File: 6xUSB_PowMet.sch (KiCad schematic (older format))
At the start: 56 parts, among them IC1 ATMEGA32-M, P1 USB_A, P2 USB_A, P3 USB_A, P4 USB_A, P5 USB_A, P6 USB_A, P7 CONN_01X08, P8 CONN_01X03, P9 CONN_01X02, U1 LM1117MP-2.5, U2 LT6106, U3 LT6106, U4 LT6106, U5 LT6106, U6 LT6106, U7 LT6106

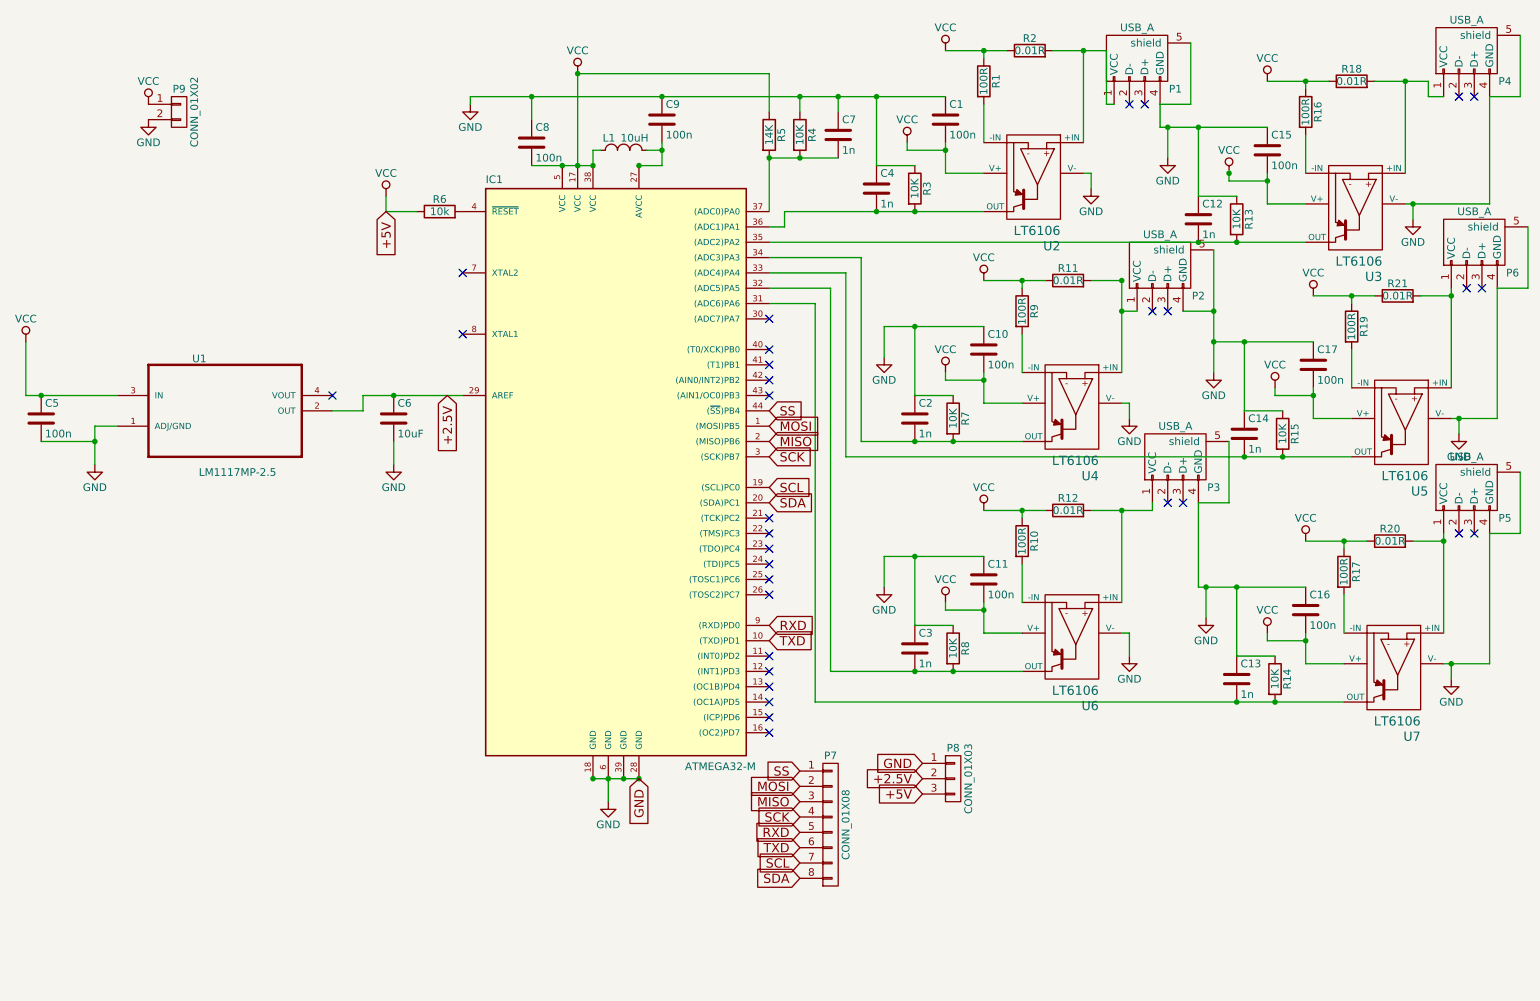
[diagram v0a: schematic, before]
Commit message: Schematic updates
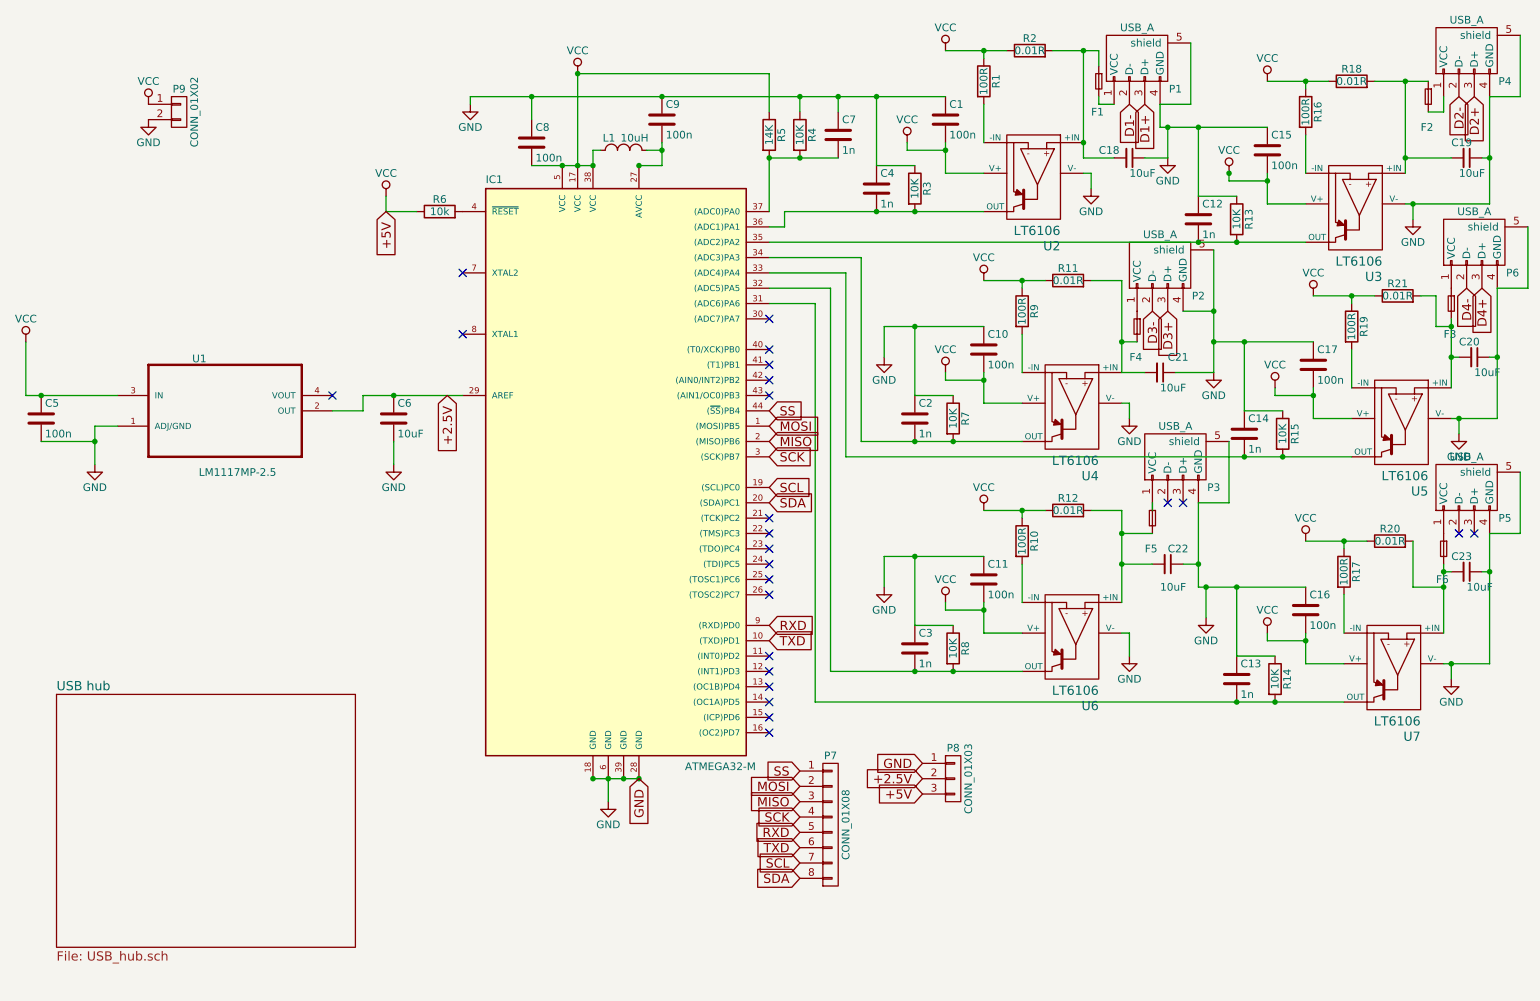
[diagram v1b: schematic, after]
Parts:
- added C18, C19, C20, C21, C22, C23: 10uF, Capacitors_SMD:C_0805_HandSoldering, symbol C_Small
- added F1, F2, F3, F4, F5, F6: F_Small, Fuse_Holders_and_Fuses:Fuse_SMD1206_HandSoldering, symbol F_Small
- P1, P2, P3, P4, P5, P6: footprint Connect:USB_A_Vertical -> USB-A_vertical1:USB_A_Vertical
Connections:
- net GND: now also C18.1, C19.1, C20.1, C21.1, C22.1, C23.1
- net at R2.2, U2.4 (+IN): now also C18.2, F1.1; no longer P1.1 (VCC)
- net at R18.2, U3.4 (+IN): now also C19.2, F2.1; no longer P4.1 (VCC)
- net at R11.2, U4.4 (+IN): now also C21.2, F4.2; no longer P2.1 (VCC)
- net at R21.2, U5.4 (+IN): now also C20.2, F3.2; no longer P6.1 (VCC)
- net at R12.2, U6.4 (+IN): now also C22.2, F5.2; no longer P3.1 (VCC)
- net at R20.2, U7.4 (+IN): now also C23.2, F6.2; no longer P5.1 (VCC)
- net D1-: now reaches P1.2 (D-)
- net D1+: now reaches P1.3 (D+)
- net D2-: now reaches P4.2 (D-)
- net D2+: now reaches P4.3 (D+)
- net D3-: now reaches P2.2 (D-)
- net D3+: now reaches P2.3 (D+)
- net D4-: now reaches P6.2 (D-)
- net D4+: now reaches P6.3 (D+)
- new net: F1.2, P1.1 (VCC)
- new net: F2.2, P4.1 (VCC)
- new net: F4.1, P2.1 (VCC)
- new net: F3.1, P6.1 (VCC)
- new net: F6.1, P5.1 (VCC)
- new net: F5.1, P3.1 (VCC)
- no-connect marks 32 -> 24

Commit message: Schematic updates
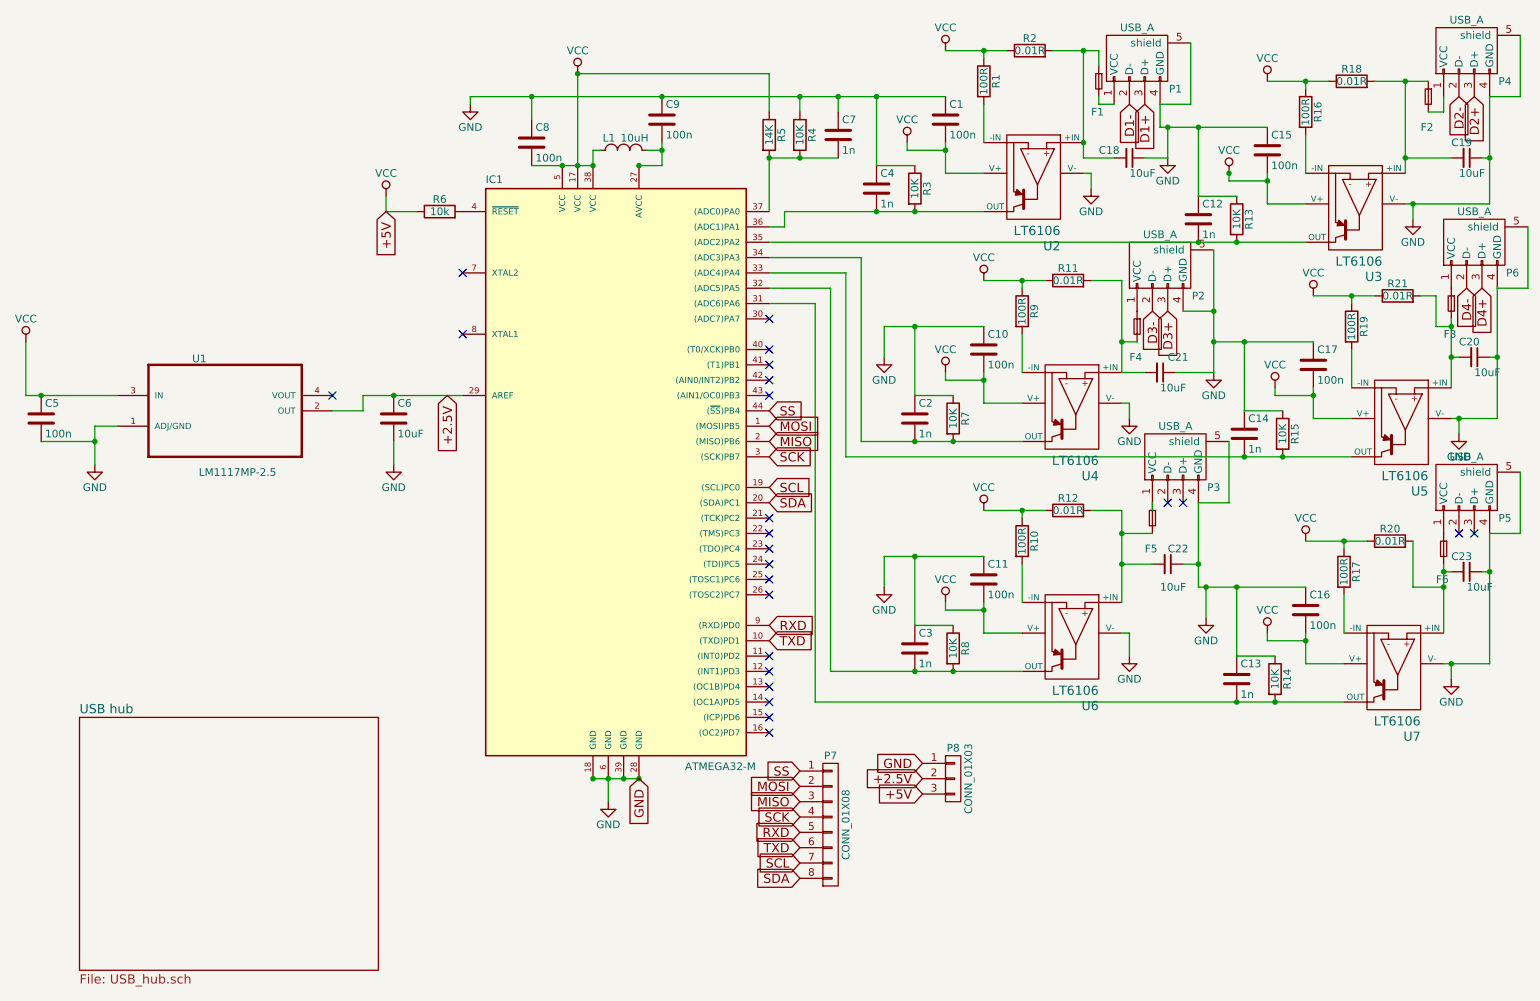
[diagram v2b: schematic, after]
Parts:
- removed P9: CONN_01X02, Connect:BARREL_JACK, symbol CONN_01X02
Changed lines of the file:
@@
 EESchema Schematic File Version 2
+LIBS:TPS5450-EP_DDA_8
 LIBS:power
 LIBS:device
@@
 LIBS:valves
 LIBS:tm-kicad-lib
+LIBS:TPS5450_DDA_8
+LIBS:tom_kicad
 LIBS:6xUSB_PowMet-cache
 EELAYER 25 0
@@
 $EndComp
 $Comp
-L GND #PWR01
+L GND #PWR7
 U 1 1 570DF0BB
 P 4850 6150
-F 0 "#PWR01" H 4850 5900 50  0001 C CNN
+F 0 "#PWR7" H 4850 5900 50  0001 C CNN
 F 1 "GND" H 4850 6000 50  0000 C CNN
 F 2 "" H 4850 6150 50  0000 C CNN
@@
 $EndComp
 $Comp
-L VCC #PWR02
+L VCC #PWR6
 U 1 1 570DF28E
 P 4650 1400
-F 0 "#PWR02" H 4650 1250 50  0001 C CNN
+F 0 "#PWR6" H 4650 1250 50  0001 C CNN
 F 1 "VCC" H 4650 1550 50  0000 C CNN
 F 2 "" H 4650 1400 50  0000 C CNN
@@
 $EndComp
 $Comp
-L VCC #PWR03
+L VCC #PWR1
 U 1 1 570E34BF
 P 1050 3150
-F 0 "#PWR03" H 1050 3000 50  0001 C CNN
+F 0 "#PWR1" H 1050 3000 50  0001 C CNN
 F 1 "VCC" H 1050 3300 50  0000 C CNN
 F 2 "" H 1050 3150 50  0000 C CNN
@@
 $EndComp
 $Comp
-L VCC #PWR04
+L VCC #PWR3
 U 1 1 570E3ABE
 P 3400 2200
-F 0 "#PWR04" H 3400 2050 50  0001 C CNN
+F 0 "#PWR3" H 3400 2050 50  0001 C CNN
 F 1 "VCC" H 3400 2350 50  0000 C CNN
 F 2 "" H 3400 2200 50  0000 C CNN
@@
 $EndComp
 $Comp
-L GND #PWR05
+L GND #PWR5
 U 1 1 570E43D9
 P 3950 1600
-F 0 "#PWR05" H 3950 1350 50  0001 C CNN
+F 0 "#PWR5" H 3950 1350 50  0001 C CNN
 F 1 "GND" H 3950 1450 50  0000 C CNN
 F 2 "" H 3950 1600 50  0000 C CNN
@@
 $EndComp
 $Comp
-L GND #PWR06
+L GND #PWR4
 U 1 1 570E5884
 P 3450 3950
-F 0 "#PWR06" H 3450 3700 50  0001 C CNN
+F 0 "#PWR4" H 3450 3700 50  0001 C CNN
 F 1 "GND" H 3450 3800 50  0000 C CNN
 F 2 "" H 3450 3950 50  0000 C CNN
@@
 $EndComp
 $Comp
-L VCC #PWR07
+L VCC #PWR10
 U 1 1 570E7287
 P 6800 1850
-F 0 "#PWR07" H 6800 1700 50  0001 C CNN
+F 0 "#PWR10" H 6800 1700 50  0001 C CNN
 F 1 "VCC" H 6800 2000 50  0000 C CNN
 F 2 "" H 6800 1850 50  0000 C CNN
@@
 $EndComp
 $Comp
-L VCC #PWR08
+L VCC #PWR11
 U 1 1 570E756C
 P 7050 1250
-F 0 "#PWR08" H 7050 1100 50  0001 C CNN
+F 0 "#PWR11" H 7050 1100 50  0001 C CNN
 F 1 "VCC" H 7050 1400 50  0000 C CNN
 F 2 "" H 7050 1250 50  0000 C CNN
@@
 $EndComp
 $Comp
-L GND #PWR09
+L GND #PWR16
 U 1 1 570E7821
 P 8000 2150
-F 0 "#PWR09" H 8000 1900 50  0001 C CNN
+F 0 "#PWR16" H 8000 1900 50  0001 C CNN
 F 1 "GND" H 8000 2000 50  0000 C CNN
 F 2 "" H 8000 2150 50  0000 C CNN
@@
 $EndComp
 $Comp
-L VCC #PWR010
+L VCC #PWR22
 U 1 1 570E7C8D
 P 8900 2050
-F 0 "#PWR010" H 8900 1900 50  0001 C CNN
+F 0 "#PWR22" H 8900 1900 50  0001 C CNN
 F 1 "VCC" H 8900 2200 50  0000 C CNN
 F 2 "" H 8900 2050 50  0000 C CNN
@@
 $EndComp
 $Comp
-L GND #PWR011
+L GND #PWR28
 U 1 1 570E7CBD
 P 10100 2350
-F 0 "#PWR011" H 10100 2100 50  0001 C CNN
+F 0 "#PWR28" H 10100 2100 50  0001 C CNN
 F 1 "GND" H 10100 2200 50  0000 C CNN
 F 2 "" H 10100 2350 50  0000 C CNN
@@
 $EndComp
 $Comp
-L GND #PWR012
+L GND #PWR19
 U 1 1 570EDB61
 P 8500 1950
-F 0 "#PWR012" H 8500 1700 50  0001 C CNN
+F 0 "#PWR19" H 8500 1700 50  0001 C CNN
 F 1 "GND" H 8500 1800 50  0000 C CNN
 F 2 "" H 8500 1950 50  0000 C CNN
@@
 $EndComp
 $Comp
-L VCC #PWR013
+L VCC #PWR14
 U 1 1 570EDEF6
 P 7300 2750
-F 0 "#PWR013" H 7300 2600 50  0001 C CNN
+F 0 "#PWR14" H 7300 2600 50  0001 C CNN
 F 1 "VCC" H 7300 2900 50  0000 C CNN
 F 2 "" H 7300 2750 50  0000 C CNN
@@
 $EndComp
 $Comp
-L GND #PWR014
+L GND #PWR17
 U 1 1 570EDF0F
 P 8250 3650
-F 0 "#PWR014" H 8250 3400 50  0001 C CNN
+F 0 "#PWR17" H 8250 3400 50  0001 C CNN
 F 1 "GND" H 8250 3500 50  0000 C CNN
 F 2 "" H 8250 3650 50  0000 C CNN
@@
 $EndComp
 $Comp
-L GND #PWR015
+L GND #PWR8
 U 1 1 570EDF17
 P 6650 3250
-F 0 "#PWR015" H 6650 3000 50  0001 C CNN
+F 0 "#PWR8" H 6650 3000 50  0001 C CNN
 F 1 "GND" H 6650 3100 50  0000 C CNN
 F 2 "" H 6650 3250 50  0000 C CNN
@@
 $EndComp
 $Comp
-L VCC #PWR016
+L VCC #PWR25
 U 1 1 570EE269
 P 9200 3450
-F 0 "#PWR016" H 9200 3300 50  0001 C CNN
+F 0 "#PWR25" H 9200 3300 50  0001 C CNN
 F 1 "VCC" H 9200 3600 50  0000 C CNN
 F 2 "" H 9200 3450 50  0000 C CNN
@@
 $EndComp
 $Comp
-L VCC #PWR017
+L VCC #PWR27
 U 1 1 570EE27F
 P 9450 2850
-F 0 "#PWR017" H 9450 2700 50  0001 C CNN
+F 0 "#PWR27" H 9450 2700 50  0001 C CNN
 F 1 "VCC" H 9450 3000 50  0000 C CNN
 F 2 "" H 9450 2850 50  0000 C CNN
@@
 $EndComp
 $Comp
-L GND #PWR018
+L GND #PWR30
 U 1 1 570EE298
 P 10400 3750
-F 0 "#PWR018" H 10400 3500 50  0001 C CNN
+F 0 "#PWR30" H 10400 3500 50  0001 C CNN
 F 1 "GND" H 10400 3600 50  0000 C CNN
 F 2 "" H 10400 3750 50  0000 C CNN
@@
 $EndComp
 $Comp
-L GND #PWR019
+L GND #PWR21
 U 1 1 570EE2A0
 P 8800 3350
-F 0 "#PWR019" H 8800 3100 50  0001 C CNN
+F 0 "#PWR21" H 8800 3100 50  0001 C CNN
 F 1 "GND" H 8800 3200 50  0000 C CNN
 F 2 "" H 8800 3350 50  0000 C CNN
@@
 $EndComp
 $Comp
-L VCC #PWR020
+L VCC #PWR13
 U 1 1 570EE6C7
 P 7050 4850
-F 0 "#PWR020" H 7050 4700 50  0001 C CNN
+F 0 "#PWR13" H 7050 4700 50  0001 C CNN
 F 1 "VCC" H 7050 5000 50  0000 C CNN
 F 2 "" H 7050 4850 50  0000 C CNN
@@
 $EndComp
 $Comp
-L VCC #PWR021
+L VCC #PWR15
 U 1 1 570EE6DD
 P 7300 4250
-F 0 "#PWR021" H 7300 4100 50  0001 C CNN
+F 0 "#PWR15" H 7300 4100 50  0001 C CNN
 F 1 "VCC" H 7300 4400 50  0000 C CNN
 F 2 "" H 7300 4250 50  0000 C CNN
@@
 $EndComp
 $Comp
-L GND #PWR022
+L GND #PWR18
 U 1 1 570EE6F6
 P 8250 5200
-F 0 "#PWR022" H 8250 4950 50  0001 C CNN
+F 0 "#PWR18" H 8250 4950 50  0001 C CNN
 F 1 "GND" H 8250 5050 50  0000 C CNN
 F 2 "" H 8250 5200 50  0000 C CNN
@@
 $EndComp
 $Comp
-L VCC #PWR023
+L VCC #PWR26
 U 1 1 570EEA49
 P 9400 4450
-F 0 "#PWR023" H 9400 4300 50  0001 C CNN
+F 0 "#PWR26" H 9400 4300 50  0001 C CNN
 F 1 "VCC" H 9400 4600 50  0000 C CNN
 F 2 "" H 9400 4450 50  0000 C CNN
@@
 $EndComp
 $Comp
-L GND #PWR024
+L GND #PWR29
 U 1 1 570EEA62
 P 10350 5350
-F 0 "#PWR024" H 10350 5100 50  0001 C CNN
+F 0 "#PWR29" H 10350 5100 50  0001 C CNN
 F 1 "GND" H 10350 5200 50  0000 C CNN
 F 2 "" H 10350 5350 50  0000 C CNN
@@
 $EndComp
 $Comp
-L GND #PWR025
+L GND #PWR20
 U 1 1 570EEA6A
 P 8750 4950
-F 0 "#PWR025" H 8750 4700 50  0001 C CNN
+F 0 "#PWR20" H 8750 4700 50  0001 C CNN
 F 1 "GND" H 8750 4800 50  0000 C CNN
 F 2 "" H 8750 4950 50  0000 C CNN
@@
 +2.5V
 $Comp
-L GND #PWR026
+L GND #PWR9
 U 1 1 57117EE7
 P 6650 4750
-F 0 "#PWR026" H 6650 4500 50  0001 C CNN
+F 0 "#PWR9" H 6650 4500 50  0001 C CNN
 F 1 "GND" H 6650 4600 50  0000 C CNN
 F 2 "" H 6650 4750 50  0000 C CNN
@@
 $EndComp
 $Comp
-L VCC #PWR027
+L VCC #PWR24
 U 1 1 5711831B
 P 9150 5050
-F 0 "#PWR027" H 9150 4900 50  0001 C CNN
+F 0 "#PWR24" H 9150 4900 50  0001 C CNN
 F 1 "VCC" H 9150 5200 50  0000 C CNN
 F 2 "" H 9150 5050 50  0000 C CNN
@@
 NoConn ~ 3050 3500
 $Comp
-L VCC #PWR028
+L VCC #PWR23
 U 1 1 5711A464
 P 9150 1450
-F 0 "#PWR028" H 9150 1300 50  0001 C CNN
+F 0 "#PWR23" H 9150 1300 50  0001 C CNN
 F 1 "VCC" H 9150 1600 50  0000 C CNN
 F 2 "" H 9150 1450 50  0000 C CNN
@@
 $EndComp
 $Comp
-L VCC #PWR029
+L VCC #PWR12
 U 1 1 5711AABD
 P 7050 3350
-F 0 "#PWR029" H 7050 3200 50  0001 C CNN
+F 0 "#PWR12" H 7050 3200 50  0001 C CNN
 F 1 "VCC" H 7050 3500 50  0000 C CNN
 F 2 "" H 7050 3350 50  0000 C CNN
@@
 $EndComp
 $Comp
-L GND #PWR030
+L GND #PWR2
 U 1 1 5711B10D
 P 1500 3950
-F 0 "#PWR030" H 1500 3700 50  0001 C CNN
+F 0 "#PWR2" H 1500 3700 50  0001 C CNN
 F 1 "GND" H 1500 3800 50  0000 C CNN
 F 2 "" H 1500 3950 50  0000 C CNN
@@
 	1    0    0    -1
 $EndComp
-$Comp
-L CONN_01X02 P9
-U 1 1 571242B0
-P 2050 1650
-F 0 "P9" H 2050 1800 50  0000 C CNN
-F 1 "CONN_01X02" V 2150 1650 50  0000 C CNN
-F 2 "Connect:BARREL_JACK" H 2050 1650 50  0001 C CNN
-F 3 "" H 2050 1650 50  0000 C CNN
-	1    2050 1650
-	1    0    0    -1
-$EndComp
-$Comp
-L VCC #PWR031
-U 1 1 5712440B
-P 1850 1600
-F 0 "#PWR031" H 1850 1450 50  0001 C CNN
-F 1 "VCC" H 1850 1750 50  0000 C CNN
-F 2 "" H 1850 1600 50  0000 C CNN
-F 3 "" H 1850 1600 50  0000 C CNN
-	1    1850 1600
-	1    0    0    -1
-$EndComp
-$Comp
-L GND #PWR032
-U 1 1 57124699
-P 1850 1700
-F 0 "#PWR032" H 1850 1450 50  0001 C CNN
-F 1 "GND" H 1850 1550 50  0000 C CNN
-F 2 "" H 1850 1700 50  0000 C CNN
-F 3 "" H 1850 1700 50  0000 C CNN
-	1    1850 1700
-	1    0    0    -1
-$EndComp
 $Sheet
-S 1250 5450 1950 1650
+S 1400 5600 1950 1650
 U 571758E7
 F0 "USB hub" 60
@@
 Connection ~ 9400 1450
 Wire Wire Line
-	10050 2050 10050 1450
+	10050 1450 10050 2050
 Wire Wire Line
 	9850 1450 10200 1450
@@
 	10100 2350 10100 2250
 Wire Wire Line
-	10050 2250 10600 2250
+	10600 2250 10050 2250
 Wire Wire Line
 	8500 1750 8500 1950
@@
 	10400 3750 10400 3650
 Wire Wire Line
-	10350 3650 10650 3650
+	10650 3650 10350 3650
 Wire Wire Line
 	8800 2550 8800 3350
@@
 	8400 4250 8400 4200
 Wire Wire Line
-	10650 3650 10650 2800
+	10650 2800 10650 3650
 Connection ~ 10400 3650
 Wire Wire Line
@@
 Connection ~ 8750 4750
 Wire Wire Line
-	10600 2250 10600 1550
+	10600 1550 10600 2250
 Connection ~ 10100 2250
 Wire Wire Line
@@
 	10300 1650 10200 1650
 Wire Wire Line
-	10350 3450 10350 3000
+	10350 3000 10350 3450
 Wire Wire Line
 	10150 2850 10250 2850
@@
 	8200 4250 8200 4850
 Wire Wire Line
-	10300 5050 10300 4600
+	10300 4600 10300 5050
 Wire Wire Line
 	10100 4450 10100 4750
